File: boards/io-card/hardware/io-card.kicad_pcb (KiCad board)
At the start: 2 copper layers, 100 x 100 mm, 4 parts

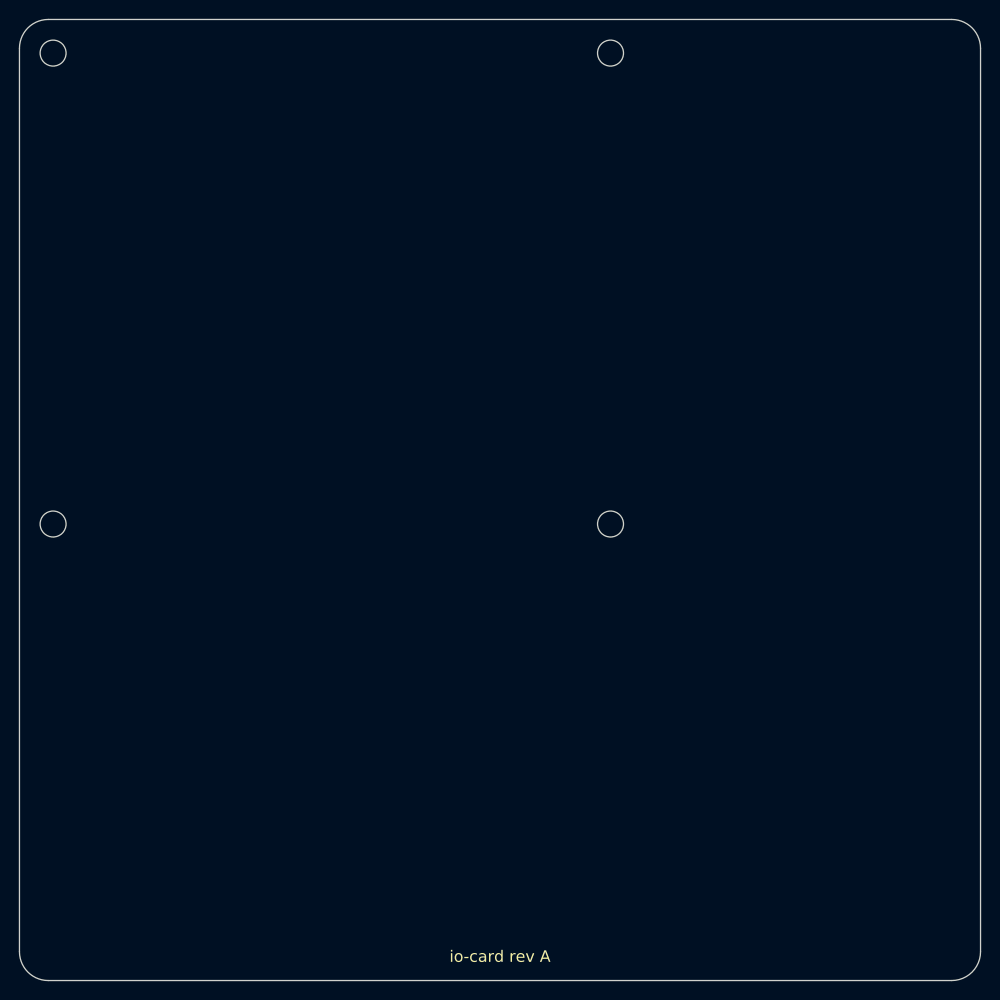
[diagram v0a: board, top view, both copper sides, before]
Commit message: io-card: external relay drivers with 24 V coil option, MC terminals, placed + routed
Relay outputs drive external coils; JP1 selects rack +12 V or an external
coil supply (up to 24 V) on J30 9/10, fused by F30 1812L110/33MR; C70 50 V.
Terminals: SPTD double-level (24.2 mm) does not fit under the next card
(~11 mm), replaced by pluggable MC 1,5/10 and /12-G-3,5 (7.7 mm, FMC plugs),
signal next to return. J40 on the top edge (LOGIC), J30 on the bottom edge
(RACK); K1/K2 straddle a 2 mm copper-free gap. AI nets in net class HV
(0.8 mm). place.py / route.py (Freerouting); check_board clean.

Co-Authored-By: Claude Opus 5.5 <noreply@anthropic.com>
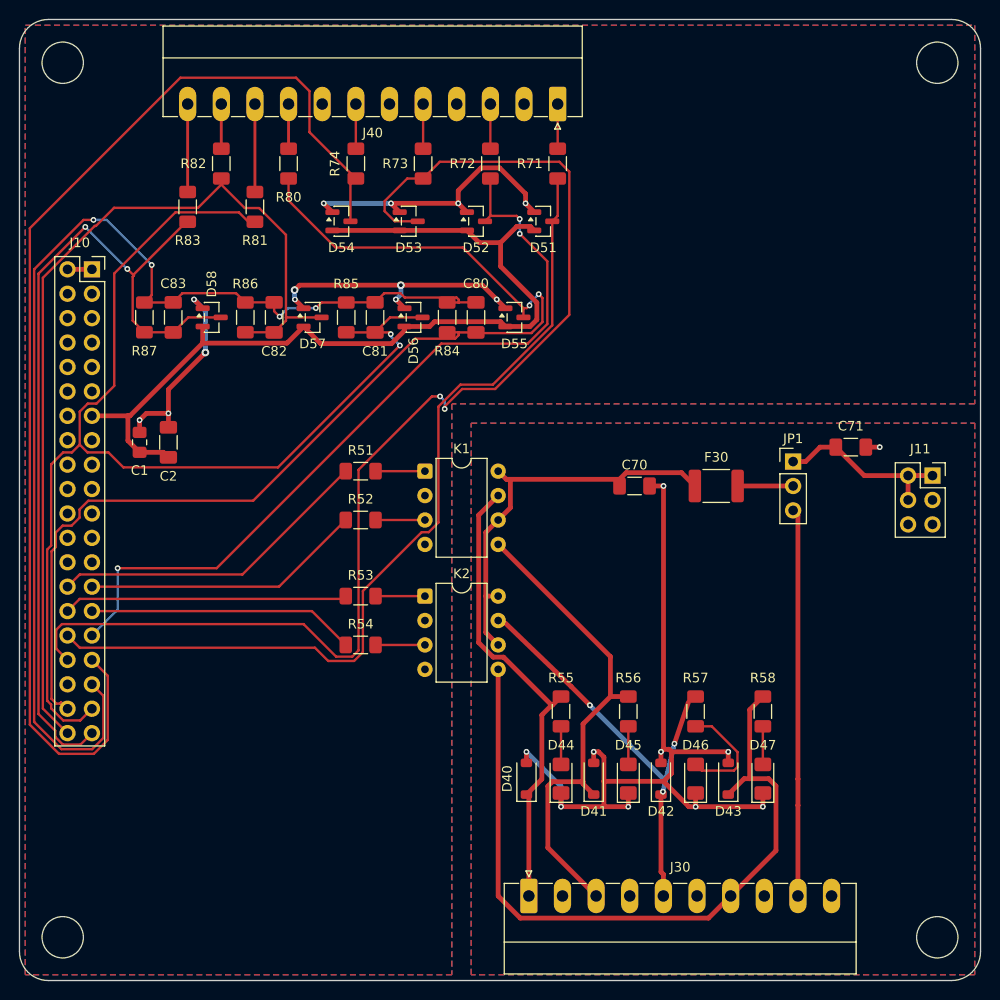
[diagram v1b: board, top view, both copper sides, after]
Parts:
- added C1: 100nF 50V X7R, Capacitor_SMD:C_0805_2012Metric_Pad1.18x1.45mm_HandSolder, F.Cu at (112.5, 144.0)
- added C2: 10uF 25V X7R, Capacitor_SMD:C_1206_3216Metric_Pad1.33x1.80mm_HandSolder, F.Cu at (115.5, 144.0)
- added C70: 4.7uF 50V X7R, Capacitor_SMD:C_1206_3216Metric_Pad1.33x1.80mm_HandSolder, F.Cu at (164.0, 148.5)
- added C71: 10uF 25V X7R, Capacitor_SMD:C_1206_3216Metric_Pad1.33x1.80mm_HandSolder, F.Cu at (186.5, 144.5)
- added C80: 100nF 50V X7R, Capacitor_SMD:C_1206_3216Metric_Pad1.33x1.80mm_HandSolder, F.Cu at (147.5, 131.0)
- added C81: 100nF 50V X7R, Capacitor_SMD:C_1206_3216Metric_Pad1.33x1.80mm_HandSolder, F.Cu at (137.0, 131.0)
- added C82: 100nF 50V X7R, Capacitor_SMD:C_1206_3216Metric_Pad1.33x1.80mm_HandSolder, F.Cu at (126.5, 131.0)
- added C83: 100nF 50V X7R, Capacitor_SMD:C_1206_3216Metric_Pad1.33x1.80mm_HandSolder, F.Cu at (116.0, 131.0)
- added D40: 1N4148W, Diode_SMD:D_SOD-123, F.Cu at (152.8, 179.0)
- added D41: 1N4148W, Diode_SMD:D_SOD-123, F.Cu at (159.8, 179.0)
- added D42: 1N4148W, Diode_SMD:D_SOD-123, F.Cu at (166.8, 179.0)
- added D43: 1N4148W, Diode_SMD:D_SOD-123, F.Cu at (173.8, 179.0)
- added D44: LED red, LED_SMD:LED_1206_3216Metric_Pad1.42x1.75mm_HandSolder, F.Cu at (156.3, 179.0)
- added D45: LED red, LED_SMD:LED_1206_3216Metric_Pad1.42x1.75mm_HandSolder, F.Cu at (163.3, 179.0)
- added D46: LED red, LED_SMD:LED_1206_3216Metric_Pad1.42x1.75mm_HandSolder, F.Cu at (170.3, 179.0)
- added D47: LED red, LED_SMD:LED_1206_3216Metric_Pad1.42x1.75mm_HandSolder, F.Cu at (177.3, 179.0)
- added D51: BAT54S, Package_TO_SOT_SMD:SOT-23, F.Cu at (154.5, 121.0)
- added D52: BAT54S, Package_TO_SOT_SMD:SOT-23, F.Cu at (147.5, 121.0)
- added D53: BAT54S, Package_TO_SOT_SMD:SOT-23, F.Cu at (140.5, 121.0)
- added D54: BAT54S, Package_TO_SOT_SMD:SOT-23, F.Cu at (133.5, 121.0)
- added D55: BAT54S, Package_TO_SOT_SMD:SOT-23, F.Cu at (151.5, 131.0)
- added D56: BAT54S, Package_TO_SOT_SMD:SOT-23, F.Cu at (141.0, 131.0)
- added D57: BAT54S, Package_TO_SOT_SMD:SOT-23, F.Cu at (130.5, 131.0)
- added D58: BAT54S, Package_TO_SOT_SMD:SOT-23, F.Cu at (120.0, 131.0)
- added F30: 1.1A 33V, Fuse:Fuse_1812_4532Metric_Pad1.30x3.40mm_HandSolder, F.Cu at (172.5, 148.5)
- added J10: STACK BUS, Connector_PinSocket_2.54mm:PinSocket_2x20_P2.54mm_Vertical, F.Cu at (107.5, 126.0)
- added J11: RACK 12V, Connector_PinSocket_2.54mm:PinSocket_2x03_P2.54mm_Vertical, F.Cu at (195.0, 147.5)
- added J30: RELAY, Connector_Phoenix_MC:PhoenixContact_MC_1,5_10-G-3.5_1x10_P3.50mm_Horizontal, F.Cu at (153.0, 191.2)
- added J40: IO, Connector_Phoenix_MC:PhoenixContact_MC_1,5_12-G-3.5_1x12_P3.50mm_Horizontal, F.Cu at (156.0, 108.8)
- added JP1: COIL SUPPLY, Connector_PinHeader_2.54mm:PinHeader_1x03_P2.54mm_Vertical, F.Cu at (180.5, 146.0)
- added K1: AQW212, Package_DIP:DIP-8_W7.62mm, F.Cu at (142.2, 147.0)
- added K2: AQW212, Package_DIP:DIP-8_W7.62mm, F.Cu at (142.2, 160.0)
- added R51: 470R, Resistor_SMD:R_1206_3216Metric_Pad1.30x1.75mm_HandSolder, F.Cu at (135.5, 147.0)
- added R52: 470R, Resistor_SMD:R_1206_3216Metric_Pad1.30x1.75mm_HandSolder, F.Cu at (135.5, 152.1)
- added R53: 470R, Resistor_SMD:R_1206_3216Metric_Pad1.30x1.75mm_HandSolder, F.Cu at (135.5, 160.0)
- added R54: 470R, Resistor_SMD:R_1206_3216Metric_Pad1.30x1.75mm_HandSolder, F.Cu at (135.5, 165.1)
- added R55: 4.7k, Resistor_SMD:R_1206_3216Metric_Pad1.30x1.75mm_HandSolder, F.Cu at (156.3, 172.0)
- added R56: 4.7k, Resistor_SMD:R_1206_3216Metric_Pad1.30x1.75mm_HandSolder, F.Cu at (163.3, 172.0)
- added R57: 4.7k, Resistor_SMD:R_1206_3216Metric_Pad1.30x1.75mm_HandSolder, F.Cu at (170.3, 172.0)
- added R58: 4.7k, Resistor_SMD:R_1206_3216Metric_Pad1.30x1.75mm_HandSolder, F.Cu at (177.3, 172.0)
- added R71: 330R, Resistor_SMD:R_1206_3216Metric_Pad1.30x1.75mm_HandSolder, F.Cu at (156.0, 115.0)
- added R72: 330R, Resistor_SMD:R_1206_3216Metric_Pad1.30x1.75mm_HandSolder, F.Cu at (149.0, 115.0)
- added R73: 330R, Resistor_SMD:R_1206_3216Metric_Pad1.30x1.75mm_HandSolder, F.Cu at (142.0, 115.0)
- added R74: 330R, Resistor_SMD:R_1206_3216Metric_Pad1.30x1.75mm_HandSolder, F.Cu at (135.0, 115.0)
- added R80: 10M, Resistor_SMD:R_1206_3216Metric_Pad1.30x1.75mm_HandSolder, F.Cu at (128.0, 115.0)
- added R81: 10M, Resistor_SMD:R_1206_3216Metric_Pad1.30x1.75mm_HandSolder, F.Cu at (124.5, 119.5)
- added R82: 10M, Resistor_SMD:R_1206_3216Metric_Pad1.30x1.75mm_HandSolder, F.Cu at (121.0, 115.0)
- added R83: 10M, Resistor_SMD:R_1206_3216Metric_Pad1.30x1.75mm_HandSolder, F.Cu at (117.5, 119.5)
- added R84: 130k, Resistor_SMD:R_1206_3216Metric_Pad1.30x1.75mm_HandSolder, F.Cu at (144.5, 131.0)
- added R85: 130k, Resistor_SMD:R_1206_3216Metric_Pad1.30x1.75mm_HandSolder, F.Cu at (134.0, 131.0)
- added R86: 130k, Resistor_SMD:R_1206_3216Metric_Pad1.30x1.75mm_HandSolder, F.Cu at (123.5, 131.0)
- added R87: 130k, Resistor_SMD:R_1206_3216Metric_Pad1.30x1.75mm_HandSolder, F.Cu at (113.0, 131.0)
- MH1, MH2, MH3, MH4: value MountingHole_2.7mm_M2.5 -> MountingHole_4.3mm_M4_Standoff7mm; footprint MountingHole:MountingHole_2.7mm_M2.5 -> Thl_Mechanical:MountingHole_4.3mm_M4_Standoff7mm
- moved MH4 54.8 mm to (195.5, 195.5)
- moved MH3 43.0 mm to (104.5, 195.5)
- moved MH2 34.0 mm to (195.5, 104.5)
- moved MH1 1.41 mm to (104.5, 104.5)
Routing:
- net /GPIO3: track 0.00 -> 127.3 mm, vias 0 -> 2
- net /AI1N: track 0.00 -> 123.7 mm, vias 0 -> 2
- net /GPIO4: track 0.00 -> 122.6 mm
- net /VMID: track 0.00 -> 121.8 mm, vias 0 -> 4
- net /AI1P: track 0.00 -> 119.0 mm, vias 0 -> 2
- net /AI2P: track 0.00 -> 97.9 mm
- net +3V3: track 0.00 -> 93.8 mm
- net /GPIO1: track 0.00 -> 92.3 mm
- net /AI2N: track 0.00 -> 90.6 mm, vias 0 -> 2
- net /GND_RACK: track 0.00 -> 89.5 mm, vias 0 -> 10
- net /GPIO2: track 0.00 -> 83.3 mm, vias 0 -> 3
- net GND: track 0.00 -> 80.2 mm, vias 0 -> 13
- net /OUT4: track 0.00 -> 78.2 mm
- net /OUT2: track 0.00 -> 51.7 mm
- net /OUT1: track 0.00 -> 48.8 mm
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- added copper zone on B.Cu, net /GND_RACK
- added copper zone on F.Cu, net /GND_RACK
- added copper zone on B.Cu, net GND
- added copper zone on F.Cu, net GND
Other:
- board text removed: "io-card rev ${REVISION}"

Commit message: io-card VMID isolation (R88 1k + C85 100 nF); relay failsafe timeout (core fw 0.4)
io-card: VMID from the core's OA5 (rated for 32 pF) now reaches the AI
dividers through R88 1k + C85 100 nF to GND (VMID_F). Rerouted, check_board
clean; AQW212 GND pins solid to the pours (starved thermal).

core: RLY takes an optional timeout=<ms> (100-3600000) for the outputs it
names; an output on with a timeout switches off unless an RLY naming it
arrives in time, and is reported in expired= until commanded again. No
timeout = no failsafe. A bare RLY does not restart timers.

Co-Authored-By: Claude Opus 5.5 <noreply@anthropic.com>
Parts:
- added C85: 100nF 50V X7R, Capacitor_SMD:C_0805_2012Metric_Pad1.18x1.45mm_HandSolder, F.Cu at (113.5, 173.5)
- added R88: 1k, Resistor_SMD:R_1206_3216Metric_Pad1.30x1.75mm_HandSolder, F.Cu at (113.5, 169.2)
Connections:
- C80 pad 2: /VMID -> /VMID_F
- C81 pad 2: /VMID -> /VMID_F
- C82 pad 2: /VMID -> /VMID_F
- C83 pad 2: /VMID -> /VMID_F
- R84 pad 2: /VMID -> /VMID_F
- R85 pad 2: /VMID -> /VMID_F
- R86 pad 2: /VMID -> /VMID_F
- R87 pad 2: /VMID -> /VMID_F
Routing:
- net /VMID: track 121.8 -> 4.41 mm, vias 4 -> 0
- net /VMID_F: track 0.00 -> 105.6 mm, vias 0 -> 4
- net GND: track 80.2 -> 140.6 mm, vias 13 -> 16
- net /GND_RACK: track 89.5 -> 40.8 mm
- net /AI1N: track 123.7 -> 87.7 mm, vias 2 -> 3
- net /GPIO3: track 127.3 -> 93.9 mm
- net /OUT4: track 78.2 -> 56.4 mm
- net /AI1P: track 119.0 -> 98.4 mm
- net /AI2N: track 90.6 -> 70.8 mm, vias 2 -> 0
- net /AI2P: track 97.9 -> 106.2 mm, vias 0 -> 1
- net /D46_A: track 11.8 -> 3.96 mm
- net /OUT3: track 43.4 -> 47.5 mm, vias 3 -> 1
- net /OUT2: track 51.7 -> 55.4 mm, vias 0 -> 1
- net +3V3: track 93.8 -> 97.4 mm
- net /GPIO4: track 122.6 -> 119.9 mm, vias 0 -> 2
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
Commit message: io-card: 4 x 0-10 V analog outputs; core fw 0.5 AO command
Hardware (boards/io-card):
- RACK-domain analog out from rack +12 V, 0 V = GND_RACK shared by all four
  and the relay returns: I2C1 -> ISO1540 -> MCP4728 (0x60, 2.048 V x 2) ->
  OPA4171 x 2.5 (10.24 V FS), 47R inside the loop + 1 nF, BAT54S clamps,
  MC78L05 for the 5 V side; J50 MC 1,5/8 on the right edge.
- Top-right corner becomes RACK (gap at x 61.5, U90 straddles it).
- Schematic sheet A2 (AO band below the original A3 area).
- Routed onto the reviewed board with route.py ao: existing tracks locked
  and returned unchanged; DAC fan-out pre-routed (net class Fine, MSOP
  pad-spacing DRC rule); Freerouting fragments on routed nets removed.
- check_board clean (ERC, DRC + schematic parity).

Firmware (boards/core): i2c.c (polled I2C1 master, bus recovery), AO
command with RLY-style optional failsafe to 0 V, ao= in IO/STATUS.
Not yet run on hardware.

Docs: requirements (core + cards is the final product; AO back on the
io-card), PROTOCOL.md, READMEs. Tools: schgen multi-unit symbols and
junctions, miniroute ground_fanout refs filter. Lib: LM2902, MC78L05_SOT89,
ISO1540, MCP4728 (+ MSOP-10, SOT-89-3).

Co-Authored-By: Claude Opus 5.5 <noreply@anthropic.com>
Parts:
- added C90: 100nF 50V X7R, Capacitor_SMD:C_0805_2012Metric_Pad1.18x1.45mm_HandSolder, F.Cu at (156.0, 137.5)
- added C91: 100nF 50V X7R, Capacitor_SMD:C_0805_2012Metric_Pad1.18x1.45mm_HandSolder, F.Cu at (166.2, 137.5)
- added C92: 100nF 50V X7R, Capacitor_SMD:C_0805_2012Metric_Pad1.18x1.45mm_HandSolder, F.Cu at (165.5, 105.5)
- added C93: 10uF 25V X7R, Capacitor_SMD:C_1206_3216Metric_Pad1.33x1.80mm_HandSolder, F.Cu at (175.0, 105.5)
- added C94: 100nF 50V X7R, Capacitor_SMD:C_0805_2012Metric_Pad1.18x1.45mm_HandSolder, F.Cu at (165.0, 128.8)
- added C95: 100nF 50V X7R, Capacitor_SMD:C_0805_2012Metric_Pad1.18x1.45mm_HandSolder, F.Cu at (168.5, 111.8)
- added C96: 1nF 50V C0G, Capacitor_SMD:C_1206_3216Metric_Pad1.33x1.80mm_HandSolder, F.Cu at (175.5, 133.0)
- added C97: 1nF 50V C0G, Capacitor_SMD:C_1206_3216Metric_Pad1.33x1.80mm_HandSolder, F.Cu at (175.5, 126.0)
- added C98: 1nF 50V C0G, Capacitor_SMD:C_1206_3216Metric_Pad1.33x1.80mm_HandSolder, F.Cu at (175.5, 119.0)
- added C99: 1nF 50V C0G, Capacitor_SMD:C_1206_3216Metric_Pad1.33x1.80mm_HandSolder, F.Cu at (175.5, 112.0)
- added D90: BAT54S, Package_TO_SOT_SMD:SOT-23, F.Cu at (186.0, 136.5)
- added D91: BAT54S, Package_TO_SOT_SMD:SOT-23, F.Cu at (186.0, 129.5)
- added D92: BAT54S, Package_TO_SOT_SMD:SOT-23, F.Cu at (186.0, 122.5)
- added D93: BAT54S, Package_TO_SOT_SMD:SOT-23, F.Cu at (186.0, 115.5)
- added J50: ANALOG OUT, Connector_Phoenix_MC:PhoenixContact_MC_1,5_8-G-3.5_1x08_P3.50mm_Horizontal, F.Cu at (191.2, 136.5)
- added R100: 47R, Resistor_SMD:R_1206_3216Metric_Pad1.30x1.75mm_HandSolder, F.Cu at (181.0, 136.5)
- added R101: 47R, Resistor_SMD:R_1206_3216Metric_Pad1.30x1.75mm_HandSolder, F.Cu at (181.0, 129.5)
- added R102: 47R, Resistor_SMD:R_1206_3216Metric_Pad1.30x1.75mm_HandSolder, F.Cu at (181.0, 122.5)
- added R103: 47R, Resistor_SMD:R_1206_3216Metric_Pad1.30x1.75mm_HandSolder, F.Cu at (181.0, 115.5)
- added R90: 4.7k, Resistor_SMD:R_1206_3216Metric_Pad1.30x1.75mm_HandSolder, F.Cu at (169.8, 134.8)
- added R91: 4.7k, Resistor_SMD:R_1206_3216Metric_Pad1.30x1.75mm_HandSolder, F.Cu at (169.8, 138.0)
- added R92: 10k 0.1%, Resistor_SMD:R_1206_3216Metric_Pad1.30x1.75mm_HandSolder, F.Cu at (175.5, 136.5)
- added R93: 10k 0.1%, Resistor_SMD:R_1206_3216Metric_Pad1.30x1.75mm_HandSolder, F.Cu at (175.5, 129.5)
- added R94: 10k 0.1%, Resistor_SMD:R_1206_3216Metric_Pad1.30x1.75mm_HandSolder, F.Cu at (175.5, 122.5)
- added R95: 10k 0.1%, Resistor_SMD:R_1206_3216Metric_Pad1.30x1.75mm_HandSolder, F.Cu at (175.5, 115.5)
- added R96: 15k 0.1%, Resistor_SMD:R_1206_3216Metric_Pad1.30x1.75mm_HandSolder, F.Cu at (181.0, 133.0)
- added R97: 15k 0.1%, Resistor_SMD:R_1206_3216Metric_Pad1.30x1.75mm_HandSolder, F.Cu at (181.0, 126.0)
- added R98: 15k 0.1%, Resistor_SMD:R_1206_3216Metric_Pad1.30x1.75mm_HandSolder, F.Cu at (181.0, 119.0)
- added R99: 15k 0.1%, Resistor_SMD:R_1206_3216Metric_Pad1.30x1.75mm_HandSolder, F.Cu at (181.0, 112.0)
- added U90: ISO1540, Package_SO:SOIC-8_3.9x4.9mm_P1.27mm, F.Cu at (161.5, 137.5)
- added U91: MC78L05, Package_TO_SOT_SMD:SOT-89-3, F.Cu at (170.0, 105.5)
- added U92: MCP4728, Package_SO:MSOP-10_3x3mm_P0.5mm, F.Cu at (168.5, 128.8)
- added U93: OPA4171, Package_SO:SOIC-14_3.9x8.7mm_P1.27mm, F.Cu at (168.5, 118.5)
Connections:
- J10 pad 15: unconnected-(J10-Pin_15-Pad15) -> /SDA
- J10 pad 16: unconnected-(J10-Pin_16-Pad16) -> /SCL
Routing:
- net /GND_RACK: track 40.8 -> 186.8 mm, vias 10 -> 27
- net +12V: track 18.9 -> 112.1 mm, vias 0 -> 2
- net /V5_AO: track 0.00 -> 74.6 mm, vias 0 -> 2
- net /SCL: track 0.00 -> 65.5 mm, vias 0 -> 3
- net /SDA: track 0.00 -> 60.8 mm, vias 0 -> 1
- net Net-(C96-Pad2): track 0.00 -> 48.4 mm
- net Net-(U93A--): track 0.00 -> 32.0 mm, vias 0 -> 2
- net Net-(U93B--): track 0.00 -> 27.4 mm, vias 0 -> 2
- net Net-(C97-Pad2): track 0.00 -> 26.3 mm, vias 0 -> 2
- net +3V3: track 97.4 -> 119.3 mm, vias 0 -> 3
- net /DAC1: track 0.00 -> 19.3 mm, vias 0 -> 2
- net /AO_SDA: track 0.00 -> 18.9 mm, vias 0 -> 2
- net Net-(U93D--): track 0.00 -> 17.4 mm
- net GND: track 140.6 -> 156.9 mm, vias 16 -> 18
- net /AO_SCL: track 0.00 -> 14.6 mm
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
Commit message: Probe test points on all fab boards; golden-board R/C/L test tool
tools/testpoints.py puts a 1.0 mm bare-copper pad (Thl_TestPoint:
TP_Probe_D1.0mm, board-only, no silkscreen) on every net of core,
can-card, io-card, serial-card and can-ssr, only on copper the net
already has (track, via or pour): no routing changes. Clear of foreign
copper, courtyards, all silkscreen, isolation gaps; 0.5 mm from the net's
own pads so the probe measures through the joint. Where nothing fits the
probe point is an SMD pad toe. Bottom-side test points where the parts
are on the bottom (can-ssr). DRC loop moves offenders; check_board clean
on all five boards, no reference texts moved or hidden.

tools/tptest.py: plan (net vs domain ground, across two-pin parts,
isolation between ground domains; powered.csv rail checklist) and run
(golden recording, compare with tolerance + golden spread, serial stream
from the planned probe helper or typed values, current.png step map).
docs/probe-test.md describes the workflow and the helper's interface.

Also: silk_tidy --only and board.json silk_keep; io-card place.py places
the AO row references; place.py scripts ignore TP footprints.

Co-Authored-By: Claude Opus 5.5 <noreply@anthropic.com>
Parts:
- added TP1: pour, Thl_TestPoint:TP_Probe_D1.0mm, F.Cu at (101.6, 108.6)
- added TP10: pour, Thl_TestPoint:TP_Probe_D1.0mm, F.Cu at (159.1, 112.1)
- added TP11: track, Thl_TestPoint:TP_Probe_D1.0mm, F.Cu at (172.2, 112.0)
- added TP12: track, Thl_TestPoint:TP_Probe_D1.0mm, F.Cu at (101.4, 127.9)
- added TP13: track, Thl_TestPoint:TP_Probe_D1.0mm, F.Cu at (120.9, 124.5)
- added TP14: track, Thl_TestPoint:TP_Probe_D1.0mm, F.Cu at (131.5, 123.9)
- added TP15: track, Thl_TestPoint:TP_Probe_D1.0mm, F.Cu at (168.0, 132.8)
- added TP16: track, Thl_TestPoint:TP_Probe_D1.0mm, F.Cu at (171.0, 131.5)
- added TP17: track, Thl_TestPoint:TP_Probe_D1.0mm, F.Cu at (110.0, 147.6)
- added TP18: track, Thl_TestPoint:TP_Probe_D1.0mm, F.Cu at (110.5, 143.0)
- added TP19: track, Thl_TestPoint:TP_Probe_D1.0mm, F.Cu at (114.6, 149.3)
- added TP2: track, Thl_TestPoint:TP_Probe_D1.0mm, F.Cu at (178.8, 109.6)
- added TP20: track, Thl_TestPoint:TP_Probe_D1.0mm, F.Cu at (138.5, 144.7)
- added TP21: track, Thl_TestPoint:TP_Probe_D1.0mm, F.Cu at (140.3, 147.0)
- added TP22: track, Thl_TestPoint:TP_Probe_D1.0mm, F.Cu at (160.6, 147.8)
- added TP23: track, Thl_TestPoint:TP_Probe_D1.0mm, F.Cu at (165.7, 140.8)
- added TP24: track, Thl_TestPoint:TP_Probe_D1.0mm, F.Cu at (178.0, 148.5)
- added TP25: track, Thl_TestPoint:TP_Probe_D1.0mm, F.Cu at (189.9, 147.5)
- added TP26: track, Thl_TestPoint:TP_Probe_D1.0mm, F.Cu at (122.6, 155.2)
- added TP27: track, Thl_TestPoint:TP_Probe_D1.0mm, F.Cu at (123.3, 157.6)
- added TP28: track, Thl_TestPoint:TP_Probe_D1.0mm, F.Cu at (125.1, 150.7)
- added TP29: track, Thl_TestPoint:TP_Probe_D1.0mm, F.Cu at (132.5, 153.6)
- added TP3: pour, Thl_TestPoint:TP_Probe_D1.0mm, F.Cu at (191.0, 101.6)
- added TP30: track, Thl_TestPoint:TP_Probe_D1.0mm, F.Cu at (140.3, 152.1)
- added TP31: track, Thl_TestPoint:TP_Probe_D1.0mm, F.Cu at (110.2, 169.2)
- added TP32: track, Thl_TestPoint:TP_Probe_D1.0mm, F.Cu at (111.5, 166.6)
- added TP33: track, Thl_TestPoint:TP_Probe_D1.0mm, F.Cu at (131.0, 160.4)
- added TP34: track, Thl_TestPoint:TP_Probe_D1.0mm, F.Cu at (131.9, 163.0)
- added TP35: track, Thl_TestPoint:TP_Probe_D1.0mm, F.Cu at (132.0, 165.1)
- added TP36: track, Thl_TestPoint:TP_Probe_D1.0mm, F.Cu at (140.3, 165.1)
- added TP37: track, Thl_TestPoint:TP_Probe_D1.0mm, F.Cu at (140.3, 160.0)
- added TP38: pour, Thl_TestPoint:TP_Probe_D1.0mm, F.Cu at (198.5, 160.6)
- added TP39: track, Thl_TestPoint:TP_Probe_D1.0mm, F.Cu at (110.5, 175.4)
- added TP4: track, Thl_TestPoint:TP_Probe_D1.0mm, F.Cu at (117.5, 111.8)
- added TP40: pour, Thl_TestPoint:TP_Probe_D1.0mm, F.Cu at (143.6, 170.1)
- added TP41: track, Thl_TestPoint:TP_Probe_D1.0mm, F.Cu at (151.7, 173.6)
- added TP42: pour, Thl_TestPoint:TP_Probe_D1.0mm, F.Cu at (148.0, 183.6)
- added TP43: track, Thl_TestPoint:TP_Probe_D1.0mm, F.Cu at (164.7, 182.4)
- added TP44: track, Thl_TestPoint:TP_Probe_D1.0mm, F.Cu at (167.0, 186.9)
- added TP45: track, Thl_TestPoint:TP_Probe_D1.0mm, F.Cu at (178.7, 186.5)
- added TP46: track, Thl_TestPoint:TP_Probe_D1.0mm, F.Cu at (181.0, 181.8)
- added TP47: pour, Thl_TestPoint:TP_Probe_D1.0mm, F.Cu at (108.6, 198.6)
- added TP48: pour, Thl_TestPoint:TP_Probe_D1.0mm, F.Cu at (191.5, 198.6)
- added TP5: track, Thl_TestPoint:TP_Probe_D1.0mm, F.Cu at (121.0, 111.7)
- added TP6: track, Thl_TestPoint:TP_Probe_D1.0mm, F.Cu at (124.5, 111.8)
- added TP7: track, Thl_TestPoint:TP_Probe_D1.0mm, F.Cu at (128.0, 111.7)
- added TP8: track, Thl_TestPoint:TP_Probe_D1.0mm, F.Cu at (142.0, 111.7)
- added TP9: track, Thl_TestPoint:TP_Probe_D1.0mm, F.Cu at (149.0, 111.7)
